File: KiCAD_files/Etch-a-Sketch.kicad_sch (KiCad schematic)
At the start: 30 parts, among them J1 Debug Connector, J2 Display / Mounting Socket, J3 Display Mounting Socket, U1 STM32L433CCTx, U2 W25Q64JV, U3 ICM-42688-P, U4 TPS61201DRC, U5 Battery Holder, U6 Adafruit 377, U7 Adafruit 377

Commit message: Finish schematic Rev1 and begin layout
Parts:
- removed U5: Battery Holder, symbol Etch_a_sketch_components:Keystone_2462
- added U5: Battery Holder, Etch_a_sketch_footprints:AA_Battery_Holder, symbol Etch_a_sketch_components:Battery_Holder
- C1, C10, C11, C12, C13, C2, C3, C4, C5, C6, C7, C8, C9: footprint (none) -> Capacitor_SMD:C_0201_0603Metric
- D1: footprint (none) -> LED_SMD:LED_0201_0603Metric
- J1: footprint (none) -> Connector_PinHeader_2.54mm:PinHeader_1x05_P2.54mm_Horizontal
- J2: footprint (none) -> Connector_PinHeader_2.54mm:PinHeader_1x14_P2.54mm_Vertical
- J3: footprint (none) -> Connector_PinHeader_2.54mm:PinHeader_1x04_P2.54mm_Vertical
- L1: footprint (none) -> SPM10040T_2R2M:IND_SPM10040T-2R2M
- R1, R2, R3, R4, R5: footprint (none) -> Resistor_SMD:R_0603_1608Metric
- U2: footprint (none) -> w25_footprints:SOIC-8_5P28X5P28_WIN
- U3: footprint (none) -> ICM_42688_P:PQFN50P300X250X97-14N
- U4: footprint (none) -> tps_footprints:DRC10_2P4X1P65
- U6, U7: value Adafruit 377 -> Adafruit 377 Rotary Encoder; footprint (none) -> Etch_a_sketch_footprints:Untitled
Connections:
- net GND: now also U6.2 (C), U6.4 (PB_1), U7.2 (C), U7.4 (PB_1), U5.2 (GND); no longer U6. (Quad_B), U7. (Quad_B)
- net QEI1_A: now also U7.1 (Quad_A); no longer U7. (Quad_B)
- net QEI1_B: now also U7.3 (Quad_B); no longer U7. (Quad_B)
- net QEI2_A: now also U6.1 (Quad_A); no longer U6. (Quad_B)
- net QEI2_B: now also U6.3 (Quad_B); no longer U6. (Quad_B)
- net at C1.1, L1.2, R1.1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: now also U5.1 (VDD)
- net at C8.1, R4.1: now also U6.5 (PB_2); no longer U6. (Quad_B)
- net at C9.1, R5.1: now also U7.5 (PB_2); no longer U7. (Quad_B)
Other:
- moved on the sheet: C13

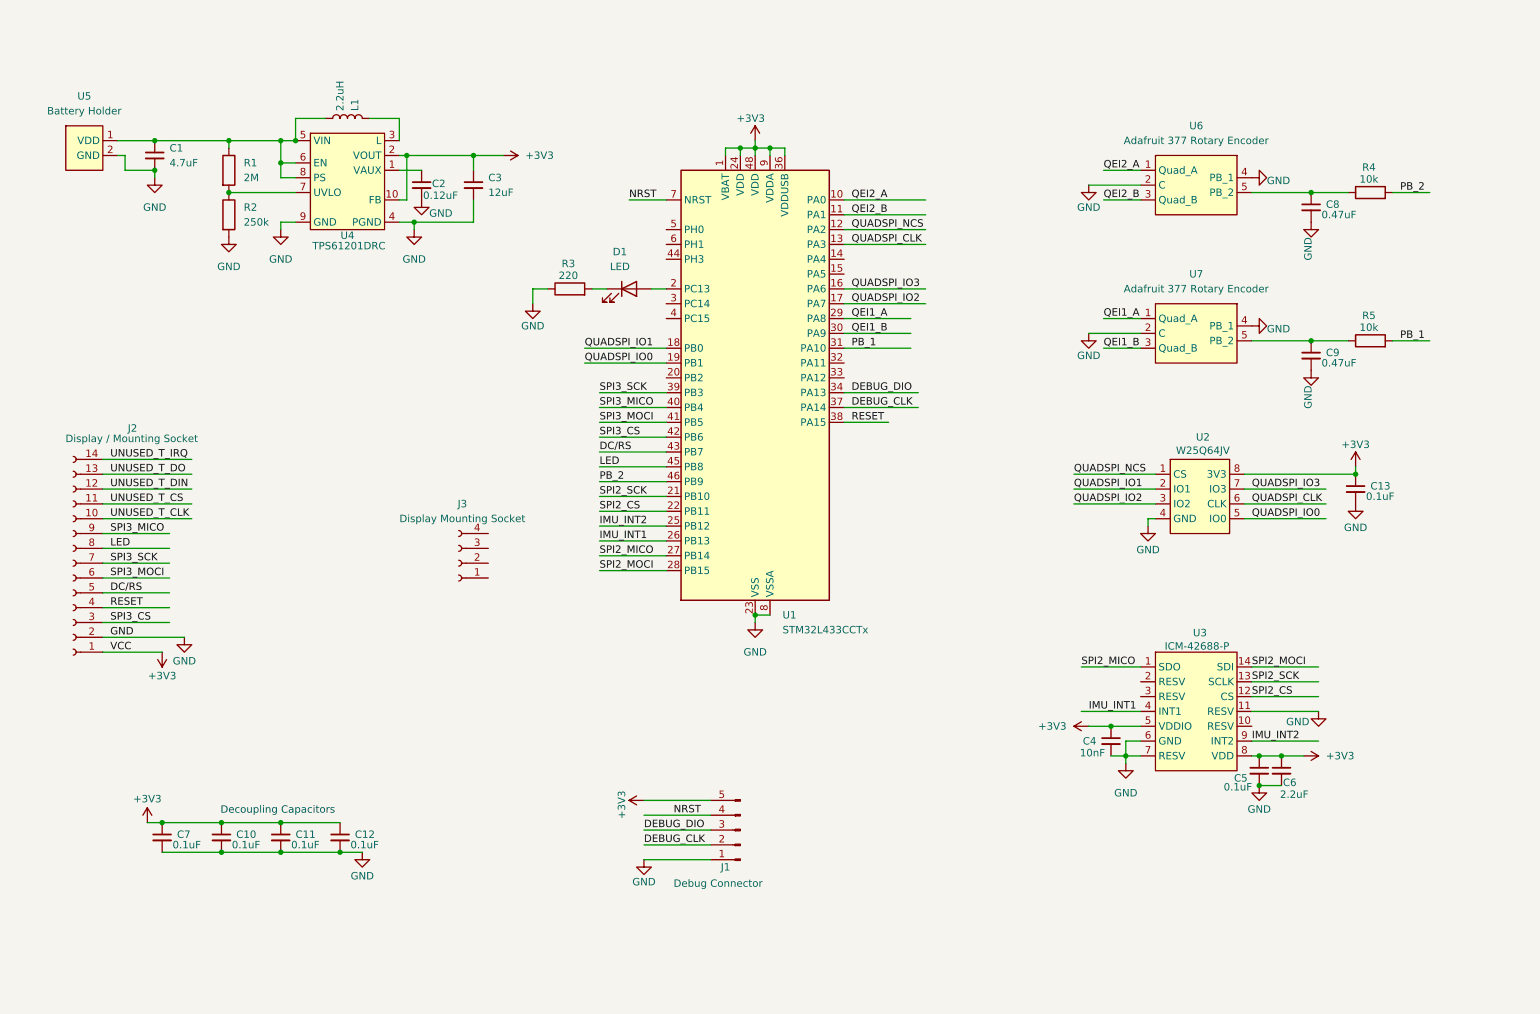
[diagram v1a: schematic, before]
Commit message: Add footprints and 3D models, initial component layout, hardware improvements
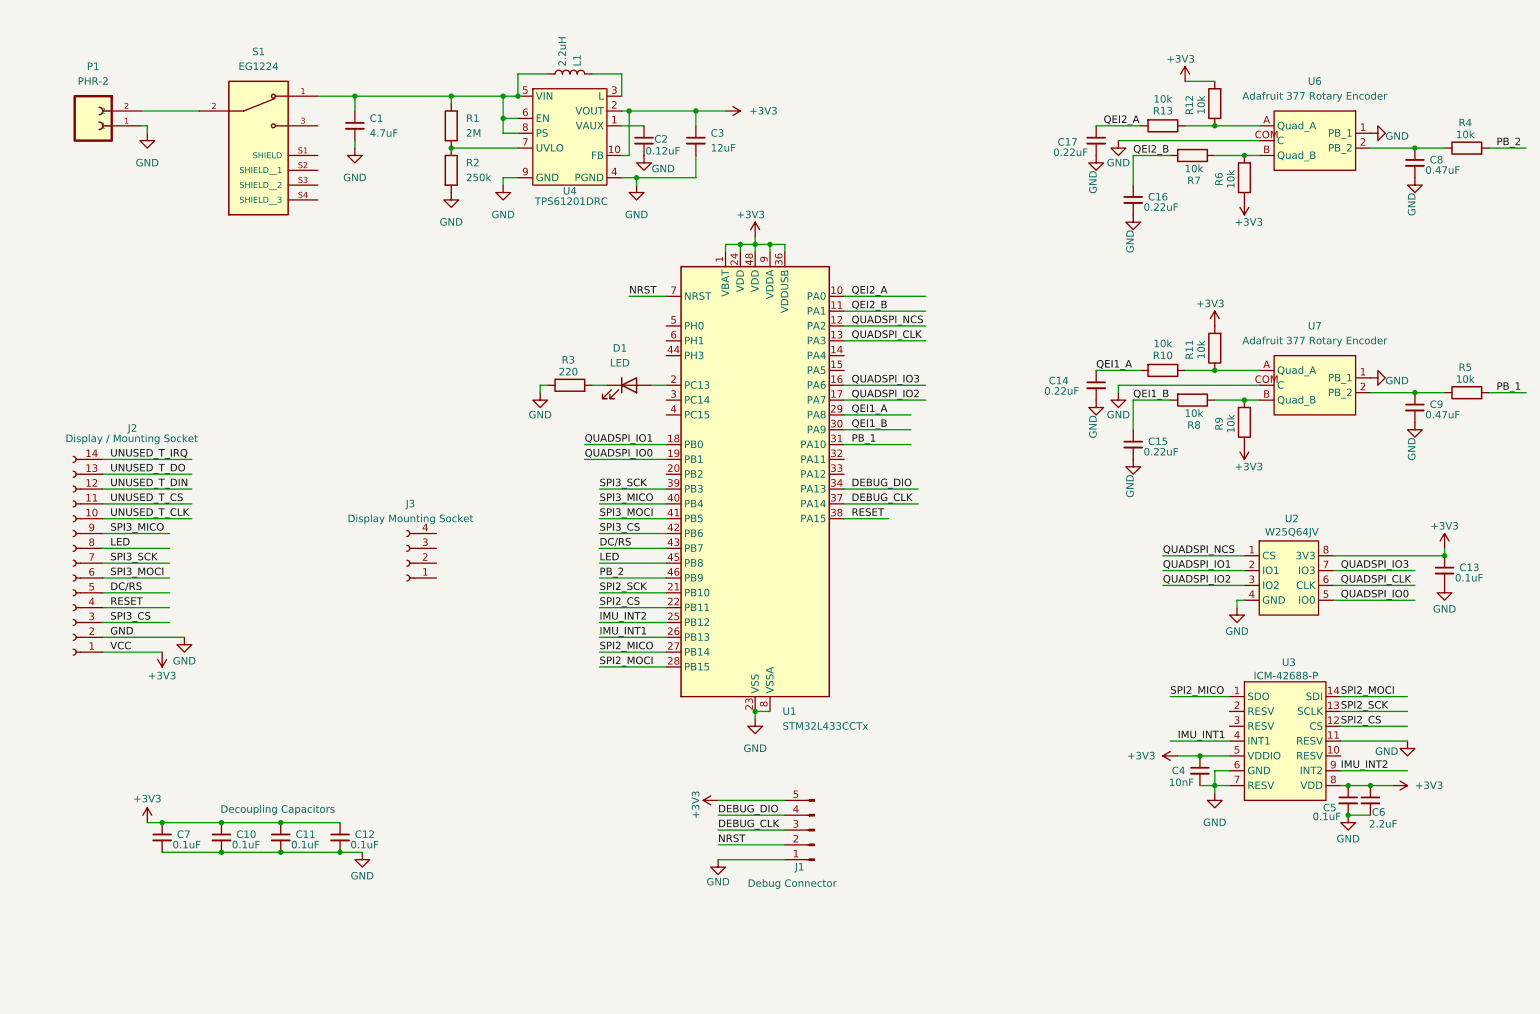
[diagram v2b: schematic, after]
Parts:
- removed U5: Battery Holder, Etch_a_sketch_footprints:AA_Battery_Holder, symbol Etch_a_sketch_components:Battery_Holder
- added C14, C15, C16, C17: 0.22uF, Capacitor_SMD:C_0201_0603Metric, symbol Device:C_Small
- added P1: PHR-2, PHR_2:JST_PHR-2, symbol PHR-2:PHR-2
- added R10, R11, R12, R13, R6, R7, R8, R9: 10k, Resistor_SMD:R_0603_1608Metric, symbol Device:R
- added S1: EG1224, EG1224:SW_EG1224, symbol EG1224:EG1224
- U4: footprint tps_footprints:DRC10_2P4X1P65 -> TPS61201DRCT:VREG_V62_16624-01YE
- U6, U7: footprint Etch_a_sketch_footprints:Untitled -> PEC11R_4215F_S0024:XDCR_PEC11R-4215F-S0024
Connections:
- net +3V3: now also R11.2, R12.2, R6.1, R9.1
- net DEBUG_CLK: now also J1.3 (Pin_3); no longer J1.2 (Pin_2)
- net DEBUG_DIO: now also J1.4 (Pin_4); no longer J1.3 (Pin_3)
- net GND: now also U6.1 (PB_1), U6.COM (C), U7.1 (PB_1), U7.COM (C), C14.2, C15.2, C16.2, C17.2, P1.1; no longer U6.2 (C), U6.4 (PB_1), U7.2 (C), U7.4 (PB_1)
- net NRST: now also J1.2 (Pin_2); no longer J1.4 (Pin_4)
- net QEI1_A: now also C14.1, R10.2; no longer U7.1 (Quad_A)
- net QEI1_B: now also C15.1, R8.2; no longer U7.3 (Quad_B)
- net QEI2_A: now also C17.1, R13.2; no longer U6.1 (Quad_A)
- net QEI2_B: now also C16.1, R7.2; no longer U6.3 (Quad_B)
- net at C9.1, R5.1: now also U7.2 (PB_2); no longer U7.5 (PB_2)
- net at C1.1, L1.2, R1.1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: now also S1.1
- net at C8.1, R4.1: now also U6.2 (PB_2); no longer U6.5 (PB_2)
- new net: R10.1, R11.1, U7.A (Quad_A)
- new net: P1.2, S1.2
- new net: R6.2, R7.1, U6.B (Quad_B)
- new net: R12.1, R13.1, U6.A (Quad_A)
- new net: R8.1, R9.2, U7.B (Quad_B)
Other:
- moved on the sheet: C1, C13, C2, C3, C4, C5, C6, C8, C9, D1, J1, J3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

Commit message: Initial PCB Layout
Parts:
- added R14, R15: 0, Resistor_SMD:R_0603_1608Metric, symbol Device:R
- L1: footprint SPM10040T_2R2M:IND_SPM10040T-2R2M -> LPS3015-222MRC:IND_LPS3015-222MRC
- U4: value TPS61201DRC -> ~
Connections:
- net +3V3: now also R15.2
- net GND: now also U3.10 (RESV), U3.2 (RESV), U3.3 (RESV), U4.11 (THRM)
- net LED: now also R14.2; no longer J2.8 (Pin_8)
- new net: J2.8 (Pin_8), R14.1, R15.1
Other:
- moved on the sheet: C1, C2, C3, L1, P1, R1, R2, S1

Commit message: PCB layout draft and clean files
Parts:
- removed P1: PHR-2, PHR_2:JST_PHR-2, symbol PHR-2:PHR-2
- added P1: 282837-2, 282837_2:TE_282837-2, symbol 282837-2:282837-2
- C1, C10, C11, C12, C13, C14, C15, C16, C17, C2, C3, C4, C5, C6, C7, C8, C9: footprint Capacitor_SMD:C_0201_0603Metric -> Capacitor_SMD:C_0603_1608Metric
- J2: footprint Connector_PinHeader_2.54mm:PinHeader_1x14_P2.54mm_Vertical -> Connector_PinSocket_2.54mm:PinSocket_1x14_P2.54mm_Vertical
- J3: footprint Connector_PinHeader_2.54mm:PinHeader_1x04_P2.54mm_Vertical -> Connector_PinSocket_2.54mm:PinSocket_1x04_P2.54mm_Vertical
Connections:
- net GND: now also P1.1
- net at S1.2: now also P1.2
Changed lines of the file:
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@@
 	(wire
 		(pts
-			(xy 40.894 33.02) (xy 50.8 33.02)
+			(xy 40.64 33.02) (xy 50.8 33.02)
 		)
 		(stroke
@@
 	(wire
 		(pts
-			(xy 41.91 36.83) (xy 41.91 35.56)
-		)
-		(stroke
-			(width 0)
-			(type default)
-		)
-	)
-	(wire
-		(pts
 			(xy 208.28 82.55) (xy 232.41 82.55)
 		)
@@
 	(wire
 		(pts
-			(xy 40.894 35.56) (xy 41.91 35.56)
+			(xy 40.64 35.56) (xy 43.18 35.56)
 		)
 		(stroke
@@
 			)
 		)
-		(property "Footprint" "Capacitor_SMD:C_0201_0603Metric"
+		(property "Footprint" "Capacitor_SMD:C_0603_1608Metric"
 			(at 77.47 35.56 0)
 			(effects
@@
 			)
 		)
-		(property "Footprint" "Capacitor_SMD:C_0201_0603Metric"
+		(property "Footprint" "Capacitor_SMD:C_0603_1608Metric"
 			(at 222.25 148.59 0)
 			(effects
@@
 	(symbol
 		(lib_id "power:GND")
-		(at 41.91 36.83 0)
+		(at 43.18 35.56 0)
 		(unit 1)
 		(exclude_from_sim no)
@@
 		(fields_autoplaced yes)
 		(property "Reference" "#PWR038"
-			(at 41.91 43.18 0)
+			(at 43.18 41.91 0)
 			(effects
 				(font
@@
 		)
 		(property "Value" "GND"
-			(at 41.91 41.91 0)
+			(at 43.18 40.64 0)
 			(effects
 				(font
@@
 		)
 		(property "Footprint" ""
-			(at 41.91 36.83 0)
+			(at 43.18 35.56 0)
 			(effects
 				(font
@@
 		)
 		(property "Datasheet" ""
-			(at 41.91 36.83 0)
+			(at 43.18 35.56 0)
 			(effects
 				(font
@@
 		)
 		(property "Description" "Power symbol creates a global label with name \"GND\" , ground"
-			(at 41.91 36.83 0)
+			(at 43.18 35.56 0)
 			(effects
 				(font
@@
 			)
 		)
-		(property "Footprint" "Capacitor_SMD:C_0201_0603Metric"
+		(property "Footprint" "Capacitor_SMD:C_0603_1608Metric"
 			(at 54.61 160.02 0)
 			(effects
@@
 			)
 		)
-		(property "Footprint" "Capacitor_SMD:C_0201_0603Metric"
+		(property "Footprint" "Capacitor_SMD:C_0603_1608Metric"
 			(at 210.82 50.8 0)
 			(effects
@@
 			)
 		)
-		(property "Footprint" "Capacitor_SMD:C_0201_0603Metric"
+		(property "Footprint" "Capacitor_SMD:C_0603_1608Metric"
 			(at 130.81 38.1 0)
 			(effects
@@
 			)
 		)
-		(property "Footprint" "Connector_PinHeader_2.54mm:PinHeader_1x04_P2.54mm_Vertical"
+		(property "Footprint" "Connector_PinSocket_2.54mm:PinSocket_1x04_P2.54mm_Vertical"
 			(at 86.36 113.03 0)
 			(effects
@@
 			)
 		)
-		(property "Footprint" "Capacitor_SMD:C_0201_0603Metric"
+		(property "Footprint" "Capacitor_SMD:C_0603_1608Metric"
 			(at 247.65 153.67 0)
 			(effects
@@
 			)
 		)
-		(property "Footprint" "Capacitor_SMD:C_0201_0603Metric"
+		(property "Footprint" "Capacitor_SMD:C_0603_1608Metric"
 			(at 204.47 82.55 0)
 			(effects
@@
 			)
 		)
-		(property "Footprint" "Capacitor_SMD:C_0201_0603Metric"
+		(property "Footprint" "Capacitor_SMD:C_0603_1608Metric"
 			(at 210.82 92.71 0)
 			(effects
@@
 			)
 		)
-		(property "Footprint" "Capacitor_SMD:C_0201_0603Metric"
+		(property "Footprint" "Capacitor_SMD:C_0603_1608Metric"
 			(at 64.77 160.02 0)
 			(effects
@@
 			)
 		)
-		(property "Footprint" "Capacitor_SMD:C_0201_0603Metric"
+		(property "Footprint" "Capacitor_SMD:C_0603_1608Metric"
 			(at 74.93 160.02 0)
 			(effects
@@
 			)
 		)
-		(property "Footprint" "Capacitor_SMD:C_0201_0603Metric"
+		(property "Footprint" "Capacitor_SMD:C_0603_1608Metric"
 			(at 139.7 38.1 0)
 			(effects
@@
 	)
 	(symbol
-		(lib_id "PHR-2:PHR-2")
-		(at 31.75 34.29 180)
-		(unit 1)
-		(exclude_from_sim no)
-		(in_bom yes)
-		(on_board yes)
-		(dnp no)
-		(fields_autoplaced yes)
-		(property "Reference" "P1"
-			(at 32.639 25.4 0)
-			(effects
-				(font
-					(size 1.27 1.27)
-				)
-			)
-		)
-		(property "Value" "PHR-2"
-			(at 32.639 27.94 0)
-			(effects
-				(font
-					(size 1.27 1.27)
-				)
-			)
-		)
-		(property "Footprint" "PHR_2:JST_PHR-2"
-			(at 31.75 34.29 0)
-			(effects
-				(font
-					(size 1.27 1.27)
-				)
-				(justify bottom)
-				(hide yes)
-			)
-		)
-		(property "Datasheet" ""
-			(at 31.75 34.29 0)
-			(effects
-				(font
-					(size 1.27 1.27)
-				)
-				(hide yes)
-			)
-		)
-		(property "Description" ""
-			(at 31.75 34.29 0)
-			(effects
-				(font
-					(size 1.27 1.27)
-				)
-				(hide yes)
-			)
-		)
-		(property "MANUFACTURER" "JST"
-			(at 31.75 34.29 0)
-			(effects
-				(font
-					(size 1.27 1.27)
-				)
-				(justify bottom)
-				(hide yes)
-			)
-		)
-		(pin "2"
-		)
-		(pin "1"
-		)
-		(instances
-			(project ""
-				(path "/98bd81b0-c975-4429-861d-532e079be58c"
-					(reference "P1")
-					(unit 1)
-				)
-			)
-		)
-	)
-	(symbol
 		(lib_id "power:GND")
 		(at 210.82 53.34 0)
@@
 			)
 		)
-		(property "Footprint" "Capacitor_SMD:C_0201_0603Metric"
+		(property "Footprint" "Capacitor_SMD:C_0603_1608Metric"
 			(at 259.08 44.45 0)
 			(effects
@@
 			)
 		)
-		(property "Footprint" "Capacitor_SMD:C_0201_0603Metric"
+		(property "Footprint" "Capacitor_SMD:C_0603_1608Metric"
 			(at 204.47 40.64 0)
 			(effects
@@
 			)
 		)
-		(property "Footprint" "Capacitor_SMD:C_0201_0603Metric"
+		(property "Footprint" "Capacitor_SMD:C_0603_1608Metric"
 			(at 251.46 153.67 0)
 			(effects
@@
 			)
 		)
-		(property "Footprint" "Connector_PinHeader_2.54mm:PinHeader_1x14_P2.54mm_Vertical"
+		(property "Footprint" "Connector_PinSocket_2.54mm:PinSocket_1x14_P2.54mm_Vertical"
 			(at 29.21 113.03 0)
 			(effects
@@
 	)
 	(symbol
+		(lib_id "282837-2:282837-2")
+		(at 33.02 35.56 180)
+		(unit 1)
+		(exclude_from_sim no)
+		(in_bom yes)
+		(on_board yes)
+		(dnp no)
+		(fields_autoplaced yes)
+		(property "Reference" "P1"
+			(at 33.02 25.4 0)
+			(effects
+				(font
+					(size 1.27 1.27)
+				)
+			)
+		)
+		(property "Value" "282837-2"
+			(at 33.02 27.94 0)
+			(effects
+				(font
+					(size 1.27 1.27)
+				)
+			)
+		)
+		(property "Footprint" "282837_2:TE_282837-2"
+			(at 33.02 35.56 0)
+			(effects
+				(font
+					(size 1.27 1.27)
+				)
+				(justify bottom)
+				(hide yes)
+			)
+		)
+		(property "Datasheet" ""
+			(at 33.02 35.56 0)
+			(effects
+				(font
+					(size 1.27 1.27)
+				)
+				(hide yes)
+			)
+		)
+		(property "Description" ""
+			(at 33.02 35.56 0)
+			(effects
+				(font
+					(size 1.27 1.27)
+				)
+				(hide yes)
+			)
+		)
+		(property "MF" "On Shore"
+			(at 33.02 35.56 0)
+			(effects
+				(font
+					(size 1.27 1.27)
+				)
+				(justify bottom)
+				(hide yes)
+			)
+		)
+		(property "DESCRIPTION" "TERMINAL BLOCK 3.5MM 2POS PCB"
+			(at 33.02 35.56 0)
+			(effects
+				(font
+					(size 1.27 1.27)
+				)
+				(justify bottom)
+				(hide yes)
+			)
+		)
+		(property "PACKAGE" "None"
+			(at 33.02 35.56 0)
+			(effects
+				(font
+					(size 1.27 1.27)
+				)
+				(justify bottom)
+				(hide yes)
+			)
+		)
+		(property "PRICE" "0.28 USD"
+			(at 33.02 35.56 0)
+			(effects
+				(font
+					(size 1.27 1.27)
+				)
+				(justify bottom)
+				(hide yes)
+			)
+		)
+		(property "PARTREV" "G3"
+			(at 33.02 35.56 0)
+			(effects
+				(font
+					(size 1.27 1.27)
+				)
+				(justify bottom)
+				(hide yes)
+			)
+		)
+		(property "MP" "OSTTE020104"
+			(at 33.02 35.56 0)
+			(effects
+				(font
+					(size 1.27 1.27)
+				)
+				(justify bottom)
+				(hide yes)
+			)
+		)
+		(property "AVAILABILITY" "Good"
+			(at 33.02 35.56 0)
+			(effects
+				(font
+					(size 1.27 1.27)
+				)
+				(justify bottom)
+				(hide yes)
+			)
+		)
+		(pin "2"
+		)
+		(pin "1"
+		)
+		(instances
+			(project ""
+				(path "/98bd81b0-c975-4429-861d-532e079be58c"
+					(reference "P1")
+					(unit 1)
+				)
+			)
+		)
+	)
+	(symbol
 		(lib_id "Device:C_Small")
 		(at 264.16 114.3 0)
@@
 			)
 		)
-		(property "Footprint" "Capacitor_SMD:C_0201_0603Metric"
+		(property "Footprint" "Capacitor_SMD:C_0603_1608Metric"
 			(at 264.16 114.3 0)
 			(effects
@@
 			)
 		)
-		(property "Footprint" "Capacitor_SMD:C_0201_0603Metric"
+		(property "Footprint" "Capacitor_SMD:C_0603_1608Metric"
 			(at 44.45 160.02 0)
 			(effects
@@
 			)
 		)
-		(property "Footprint" "Capacitor_SMD:C_0201_0603Metric"
+		(property "Footprint" "Capacitor_SMD:C_0603_1608Metric"
 			(at 259.08 86.36 0)
 			(effects

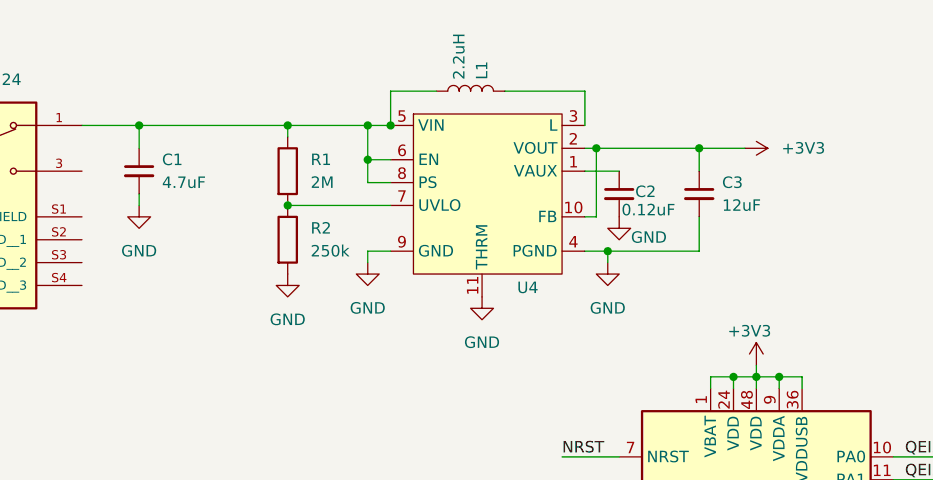
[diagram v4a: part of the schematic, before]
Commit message: Final KiCAD updates, and begin driver developpment
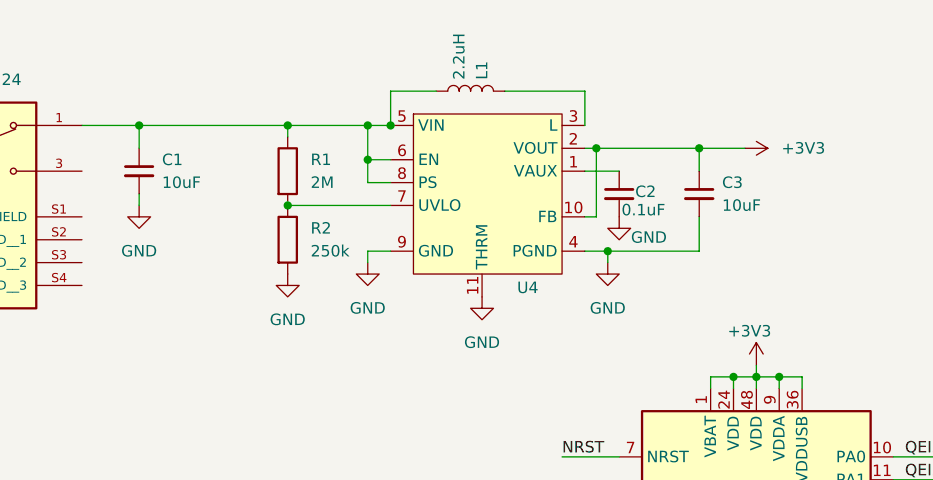
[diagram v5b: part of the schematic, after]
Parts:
- C1: value 4.7uF -> 10uF
- C2: value 0.12uF -> 0.1uF
- C3: value 12uF -> 10uF
- P1: footprint 282837_2:TE_282837-2 -> Connector_JST:JST_PH_B2B-PH-K_1x02_P2.00mm_Vertical
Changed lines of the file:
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@@
 			)
 		)
-		(property "Value" "4.7uF"
+		(property "Value" "10uF"
 			(at 80.01 36.8362 0)
 			(effects
@@
 			)
 		)
-		(property "Value" "0.12uF"
+		(property "Value" "0.1uF"
 			(at 131.064 39.878 0)
 			(effects
@@
 			)
 		)
-		(property "Value" "12uF"
+		(property "Value" "10uF"
 			(at 142.24 39.3762 0)
 			(effects
@@
 			)
 		)
-		(property "Footprint" "282837_2:TE_282837-2"
+		(property "Footprint" "Connector_JST:JST_PH_B2B-PH-K_1x02_P2.00mm_Vertical"
 			(at 33.02 35.56 0)
 			(effects
